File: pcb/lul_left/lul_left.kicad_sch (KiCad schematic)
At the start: 76 parts, among them J1 JST Connector, J2 JST Connector, SW1 SW_Push, SW10 SW_Push, SW11 SW_Push, SW12 SW_Push, SW13 SW_Push, SW14 SW_Push, SW15 SW_Push, SW16 SW_Push, SW17 SW_Push, SW18 SW_Push, SW19 SW_Push, SW2 SW_Push, SW20 SW_Push, SW21 SW_Push, SW22 SW_Push, SW23 SW_Push, SW24 SW_Push, SW25 SW_Push, SW26 SW_Push, SW27 SW_Push, SW28 SW_Push, SW29 SW_Push, SW3 SW_Push, SW30 SW_Push, SW31 SW_Push, SW32 SW_Push, SW33 SW_Push, SW34 SW_Push, SW4 SW_Push, SW5 SW_Push, SW6 SW_Push, SW7 SW_Push, SW8 SW_Push, SW9 SW_Push, U1 nice_nano, U2 nice_nano

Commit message: switches positioned properly
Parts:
- J1, J2: footprint (none) -> Connector_JST:JST_PH_S2B-PH-K_1x02_P2.00mm_Horizontal
- SW1, SW10, SW11, SW12, SW14, SW15, SW16, SW17, SW18, SW19, SW2, SW20, SW21, SW22, SW23, SW24, SW26, SW27, SW28, SW29, SW3, SW30, SW31, SW32, SW33, SW34, SW4, SW5, SW6, SW7, SW8, SW9: footprint zzkeeb:Switch_MX-hotswap -> MX_Only:MXOnly-1U-Hotswap
- SW13, SW25: footprint zzkeeb:Switch_MX-hotswap -> MX_Only:MXOnly-1.75U-Hotswap
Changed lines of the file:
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@@
       (effects (font (size 1.27 1.27)))
     )
-    (property "Footprint" "zzkeeb:Switch_MX-hotswap" (at 41.91 129.54 0)
+    (property "Footprint" "MX_Only:MXOnly-1.75U-Hotswap" (at 41.91 129.54 0)
       (effects (font (size 1.27 1.27)) hide)
     )
@@
       (effects (font (size 1.27 1.27)))
     )
-    (property "Footprint" "zzkeeb:Switch_MX-hotswap" (at 99.06 91.44 0)
+    (property "Footprint" "MX_Only:MXOnly-1U-Hotswap" (at 99.06 91.44 0)
       (effects (font (size 1.27 1.27)) hide)
     )
@@
       (effects (font (size 1.27 1.27)))
     )
-    (property "Footprint" "zzkeeb:Switch_MX-hotswap" (at 41.91 104.14 0)
+    (property "Footprint" "MX_Only:MXOnly-1U-Hotswap" (at 41.91 104.14 0)
       (effects (font (size 1.27 1.27)) hide)
     )
@@
       (effects (font (size 1.27 1.27)))
     )
-    (property "Footprint" "zzkeeb:Switch_MX-hotswap" (at 41.91 25.4 0)
+    (property "Footprint" "MX_Only:MXOnly-1U-Hotswap" (at 41.91 25.4 0)
       (effects (font (size 1.27 1.27)) hide)
     )
@@
       (effects (font (size 1.27 1.27)))
     )
-    (property "Footprint" "zzkeeb:Switch_MX-hotswap" (at 60.96 25.4 0)
+    (property "Footprint" "MX_Only:MXOnly-1U-Hotswap" (at 60.96 25.4 0)
       (effects (font (size 1.27 1.27)) hide)
     )
@@
       (effects (font (size 1.27 1.27)))
     )
-    (property "Footprint" "zzkeeb:Switch_MX-hotswap" (at 80.01 25.4 0)
+    (property "Footprint" "MX_Only:MXOnly-1U-Hotswap" (at 80.01 25.4 0)
       (effects (font (size 1.27 1.27)) hide)
     )
@@
       (effects (font (size 1.27 1.27)))
     )
-    (property "Footprint" "zzkeeb:Switch_MX-hotswap" (at 41.91 116.84 0)
+    (property "Footprint" "MX_Only:MXOnly-1U-Hotswap" (at 41.91 116.84 0)
       (effects (font (size 1.27 1.27)) hide)
     )
@@
       (effects (font (size 1.27 1.27)))
     )
-    (property "Footprint" "zzkeeb:Switch_MX-hotswap" (at 22.86 38.1 0)
+    (property "Footprint" "MX_Only:MXOnly-1U-Hotswap" (at 22.86 38.1 0)
       (effects (font (size 1.27 1.27)) hide)
     )
@@
       (effects (font (size 1.27 1.27)))
     )
-    (property "Footprint" "zzkeeb:Switch_MX-hotswap" (at 80.01 116.84 0)
+    (property "Footprint" "MX_Only:MXOnly-1U-Hotswap" (at 80.01 116.84 0)
       (effects (font (size 1.27 1.27)) hide)
     )
@@
       (effects (font (size 1.27 1.27)))
     )
-    (property "Footprint" "zzkeeb:Switch_MX-hotswap" (at 99.06 50.8 0)
+    (property "Footprint" "MX_Only:MXOnly-1U-Hotswap" (at 99.06 50.8 0)
       (effects (font (size 1.27 1.27)) hide)
     )
@@
       (effects (font (size 1.27 1.27)))
     )
-    (property "Footprint" "zzkeeb:Switch_MX-hotswap" (at 80.01 38.1 0)
+    (property "Footprint" "MX_Only:MXOnly-1U-Hotswap" (at 80.01 38.1 0)
       (effects (font (size 1.27 1.27)) hide)
     )
@@
       (effects (font (size 1.27 1.27)))
     )
-    (property "Footprint" "zzkeeb:Switch_MX-hotswap" (at 60.96 38.1 0)
+    (property "Footprint" "MX_Only:MXOnly-1U-Hotswap" (at 60.96 38.1 0)
       (effects (font (size 1.27 1.27)) hide)
     )
@@
       (effects (font (size 1.27 1.27)))
     )
-    (property "Footprint" "zzkeeb:Switch_MX-hotswap" (at 99.06 25.4 0)
+    (property "Footprint" "MX_Only:MXOnly-1U-Hotswap" (at 99.06 25.4 0)
       (effects (font (size 1.27 1.27)) hide)
     )
@@
       (effects (font (size 1.27 1.27)))
     )
-    (property "Footprint" "zzkeeb:Switch_MX-hotswap" (at 80.01 104.14 0)
+    (property "Footprint" "MX_Only:MXOnly-1U-Hotswap" (at 80.01 104.14 0)
       (effects (font (size 1.27 1.27)) hide)
     )
@@
       (effects (font (size 1.27 1.27)))
     )
-    (property "Footprint" "zzkeeb:Switch_MX-hotswap" (at 80.01 63.5 0)
+    (property "Footprint" "MX_Only:MXOnly-1.75U-Hotswap" (at 80.01 63.5 0)
       (effects (font (size 1.27 1.27)) hide)
     )
@@
       (effects (font (size 1.27 1.27)))
     )
-    (property "Footprint" "zzkeeb:Switch_MX-hotswap" (at 41.91 91.44 0)
+    (property "Footprint" "MX_Only:MXOnly-1U-Hotswap" (at 41.91 91.44 0)
       (effects (font (size 1.27 1.27)) hide)
     )
@@
       (effects (font (size 1.27 1.27)))
     )
-    (property "Footprint" "zzkeeb:Switch_MX-hotswap" (at 60.96 116.84 0)
+    (property "Footprint" "MX_Only:MXOnly-1U-Hotswap" (at 60.96 116.84 0)
       (effects (font (size 1.27 1.27)) hide)
     )
@@
       (effects (font (size 1.27 1.27)))
     )
-    (property "Footprint" "zzkeeb:Switch_MX-hotswap" (at 22.86 116.84 0)
+    (property "Footprint" "MX_Only:MXOnly-1U-Hotswap" (at 22.86 116.84 0)
       (effects (font (size 1.27 1.27)) hide)
     )
@@
       (effects (font (size 1.27 1.27)))
     )
-    (property "Footprint" "zzkeeb:Switch_MX-hotswap" (at 99.06 104.14 0)
+    (property "Footprint" "MX_Only:MXOnly-1U-Hotswap" (at 99.06 104.14 0)
       (effects (font (size 1.27 1.27)) hide)
     )
@@
       (effects (font (size 1.27 1.27)))
     )
-    (property "Footprint" "zzkeeb:Switch_MX-hotswap" (at 99.06 116.84 0)
+    (property "Footprint" "MX_Only:MXOnly-1U-Hotswap" (at 99.06 116.84 0)
       (effects (font (size 1.27 1.27)) hide)
     )
@@
       (effects (font (size 1.27 1.27)))
     )
-    (property "Footprint" "zzkeeb:Switch_MX-hotswap" (at 80.01 91.44 0)
+    (property "Footprint" "MX_Only:MXOnly-1U-Hotswap" (at 80.01 91.44 0)
       (effects (font (size 1.27 1.27)) hide)
     )
@@
       (effects (font (size 1.27 1.27)))
     )
-    (property "Footprint" "zzkeeb:Switch_MX-hotswap" (at 99.06 38.1 0)
+    (property "Footprint" "MX_Only:MXOnly-1U-Hotswap" (at 99.06 38.1 0)
       (effects (font (size 1.27 1.27)) hide)
     )
@@
       (effects (font (size 1.27 1.27)))
     )
-    (property "Footprint" "zzkeeb:Switch_MX-hotswap" (at 80.01 50.8 0)
+    (property "Footprint" "MX_Only:MXOnly-1U-Hotswap" (at 80.01 50.8 0)
       (effects (font (size 1.27 1.27)) hide)
     )
@@
       (effects (font (size 1.27 1.27)))
     )
-    (property "Footprint" "zzkeeb:Switch_MX-hotswap" (at 22.86 129.54 0)
+    (property "Footprint" "MX_Only:MXOnly-1U-Hotswap" (at 22.86 129.54 0)
       (effects (font (size 1.27 1.27)) hide)
     )
@@
       (effects (font (size 1.27 1.27)))
     )
-    (property "Footprint" "zzkeeb:Switch_MX-hotswap" (at 60.96 91.44 0)
+    (property "Footprint" "MX_Only:MXOnly-1U-Hotswap" (at 60.96 91.44 0)
       (effects (font (size 1.27 1.27)) hide)
     )
@@
       (effects (font (size 1.27 1.27)))
     )
-    (property "Footprint" "zzkeeb:Switch_MX-hotswap" (at 60.96 50.8 0)
+    (property "Footprint" "MX_Only:MXOnly-1U-Hotswap" (at 60.96 50.8 0)
       (effects (font (size 1.27 1.27)) hide)
     )
@@
       (effects (font (size 1.27 1.27)))
     )
-    (property "Footprint" "" (at 114.3 161.29 0)
+    (property "Footprint" "Connector_JST:JST_PH_S2B-PH-K_1x02_P2.00mm_Horizontal" (at 114.3 161.29 0)
       (effects (font (size 1.27 1.27)) hide)
     )
@@
       (effects (font (size 1.27 1.27)))
     )
-    (property "Footprint" "zzkeeb:Switch_MX-hotswap" (at 41.91 38.1 0)
+    (property "Footprint" "MX_Only:MXOnly-1U-Hotswap" (at 41.91 38.1 0)
       (effects (font (size 1.27 1.27)) hide)
     )
@@
       (effects (font (size 1.27 1.27)))
     )
-    (property "Footprint" "" (at 74.93 160.02 0)
+    (property "Footprint" "Connector_JST:JST_PH_S2B-PH-K_1x02_P2.00mm_Horizontal" (at 74.93 160.02 0)
       (effects (font (size 1.27 1.27)) hide)
     )
@@
       (effects (font (size 1.27 1.27)))
     )
-    (property "Footprint" "zzkeeb:Switch_MX-hotswap" (at 22.86 25.4 0)
+    (property "Footprint" "MX_Only:MXOnly-1U-Hotswap" (at 22.86 25.4 0)
       (effects (font (size 1.27 1.27)) hide)
     )
@@
       (effects (font (size 1.27 1.27)))
     )
-    (property "Footprint" "zzkeeb:Switch_MX-hotswap" (at 22.86 91.44 0)
+    (property "Footprint" "MX_Only:MXOnly-1U-Hotswap" (at 22.86 91.44 0)
       (effects (font (size 1.27 1.27)) hide)
     )
@@
       (effects (font (size 1.27 1.27)))
     )
-    (property "Footprint" "zzkeeb:Switch_MX-hotswap" (at 60.96 104.14 0)
+    (property "Footprint" "MX_Only:MXOnly-1U-Hotswap" (at 60.96 104.14 0)
       (effects (font (size 1.27 1.27)) hide)
     )
@@
       (effects (font (size 1.27 1.27)))
     )
-    (property "Footprint" "zzkeeb:Switch_MX-hotswap" (at 22.86 104.14 0)
+    (property "Footprint" "MX_Only:MXOnly-1U-Hotswap" (at 22.86 104.14 0)
       (effects (font (size 1.27 1.27)) hide)
     )
@@
       (effects (font (size 1.27 1.27)))
     )
-    (property "Footprint" "zzkeeb:Switch_MX-hotswap" (at 99.06 63.5 0)
+    (property "Footprint" "MX_Only:MXOnly-1U-Hotswap" (at 99.06 63.5 0)
       (effects (font (size 1.27 1.27)) hide)
     )
@@
       (effects (font (size 1.27 1.27)))
     )
-    (property "Footprint" "zzkeeb:Switch_MX-hotswap" (at 22.86 50.8 0)
+    (property "Footprint" "MX_Only:MXOnly-1U-Hotswap" (at 22.86 50.8 0)
       (effects (font (size 1.27 1.27)) hide)
     )
@@
       (effects (font (size 1.27 1.27)))
     )
-    (property "Footprint" "zzkeeb:Switch_MX-hotswap" (at 41.91 50.8 0)
-      (effects (font (size 1.27 1.27)) hide)
-    )
+    (property "Footprint" "MX_Only:MXOnly-1U-Hotswap" (at 41.91 50.8 0)
+      (effects (font (size 1.27 1.27)) hide)
+    )

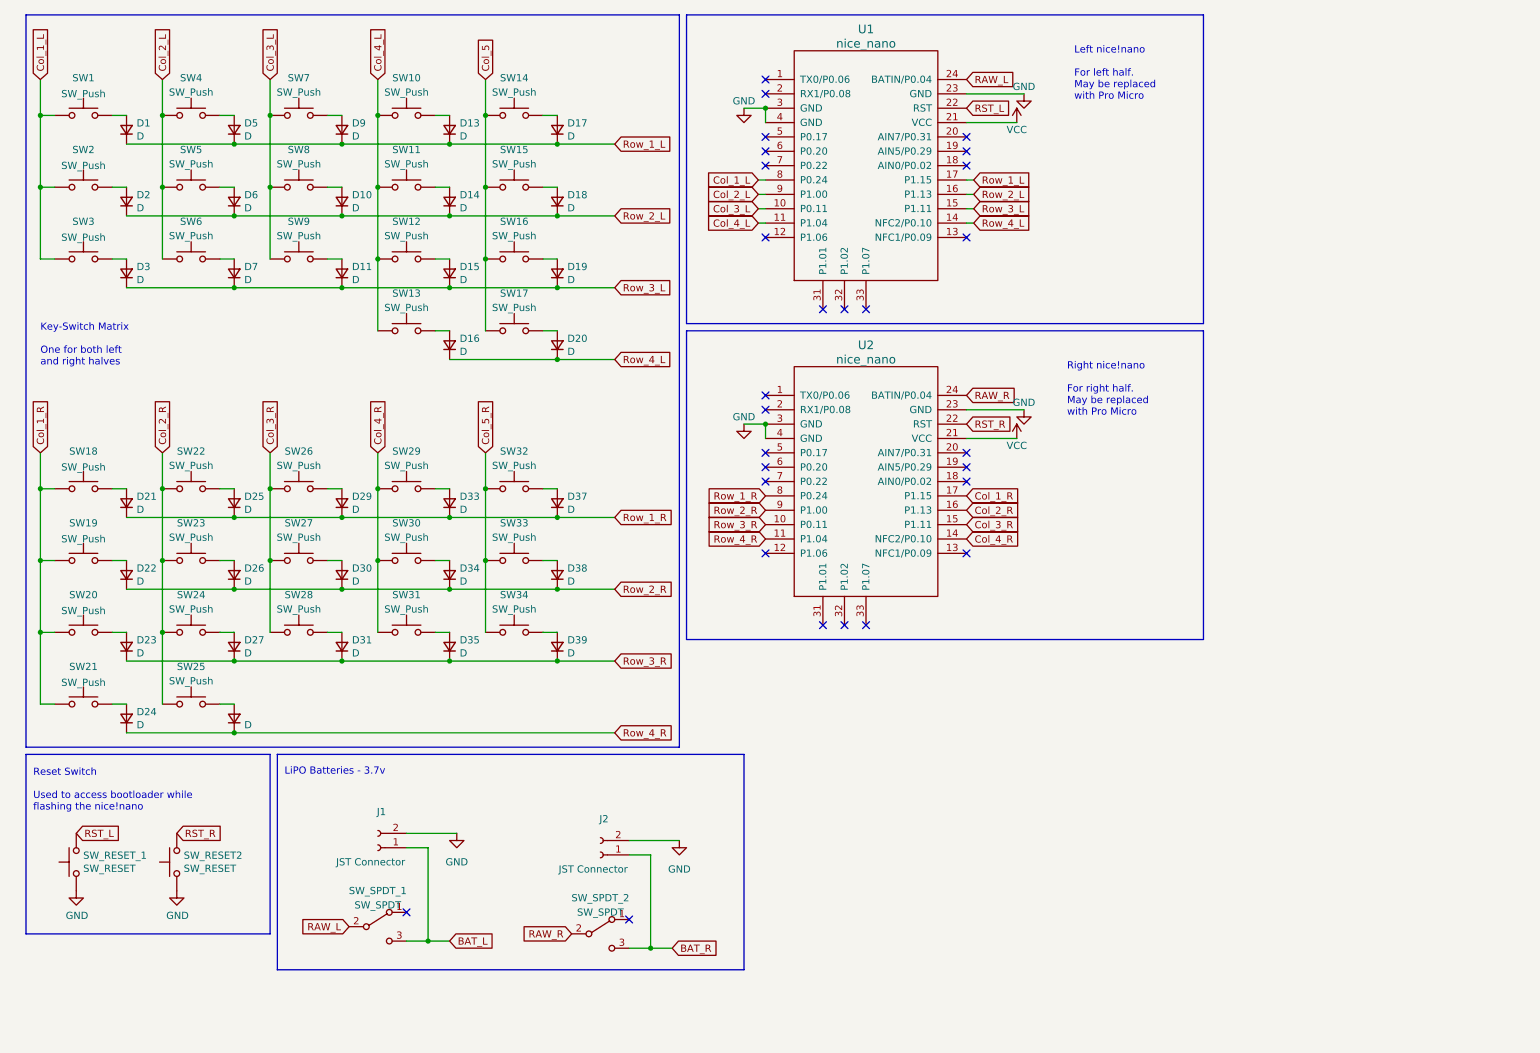
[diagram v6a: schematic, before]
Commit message: change schematic to be diode-less
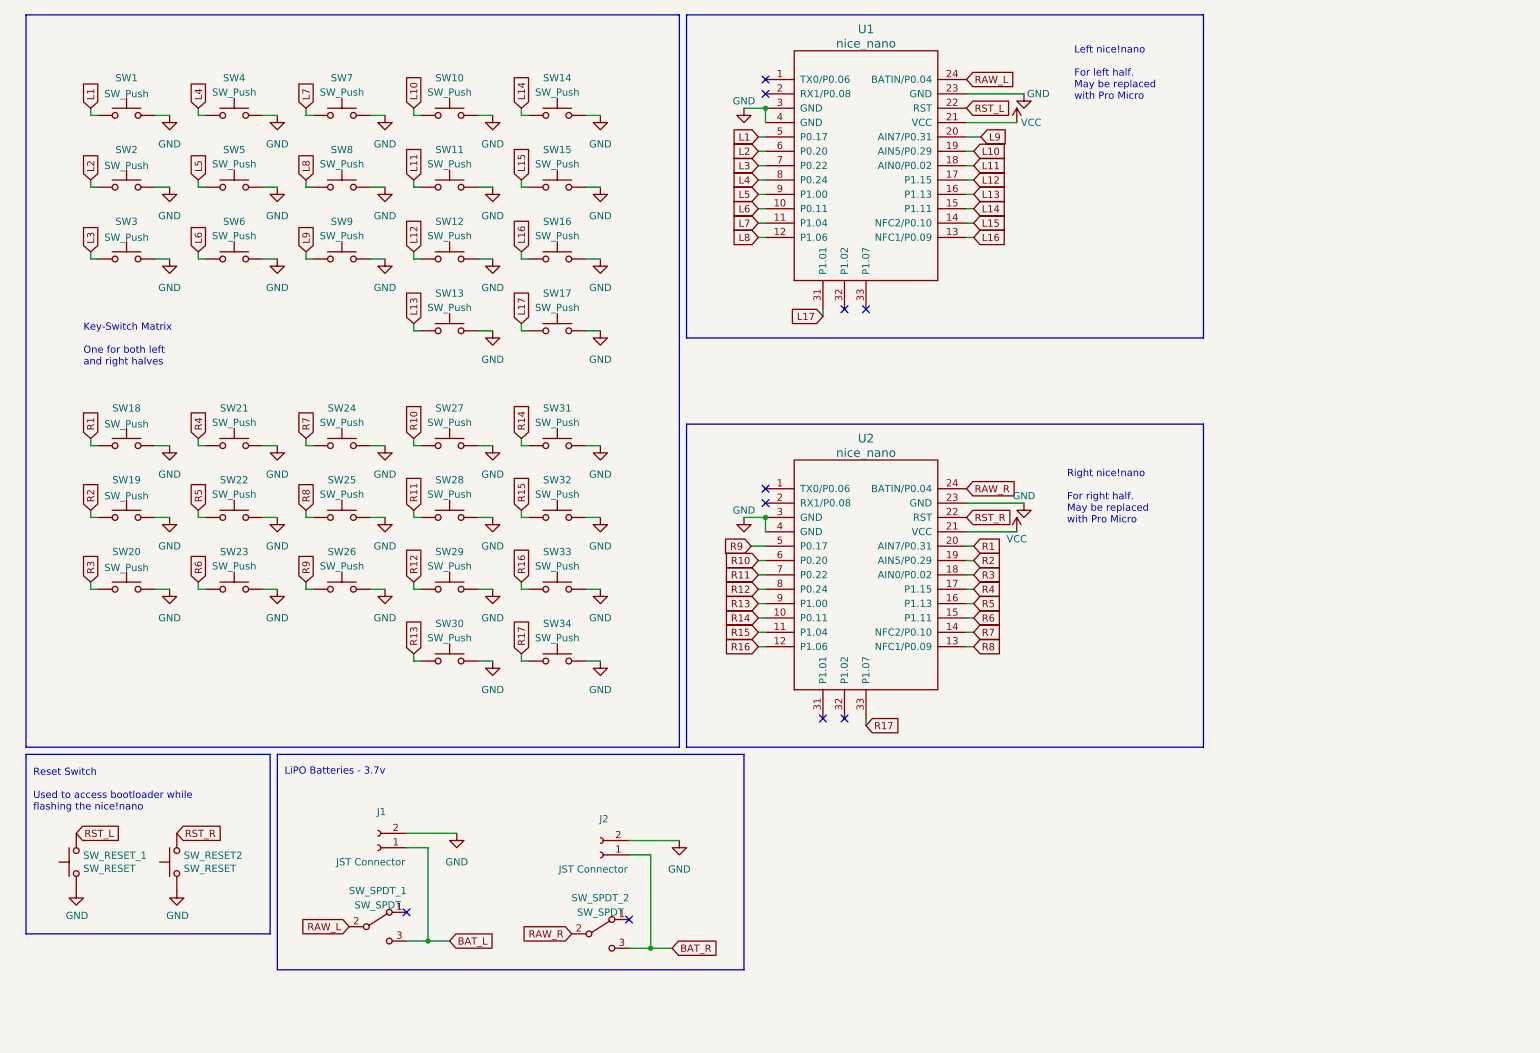
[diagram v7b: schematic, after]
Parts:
- removed D1, D10, D11, D13, D14, D15, D16, D17, D18, D19, D2, D20, D21, D22, D23, D24, D25, D26, D27, D28, D29, D3, D30, D31, D33, D34, D35, D37, D38, D39, D5, D6, D7, D9: D, Diode_SMD:D_SOD-123, symbol Device:D_Small
- SW25: footprint MX_Only:MXOnly-1.75U-Hotswap -> MX_Only:MXOnly-1U-Hotswap
- SW30: footprint MX_Only:MXOnly-1U-Hotswap -> MX_Only:MXOnly-1.75U-Hotswap
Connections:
- net GND: now also SW1.2, SW10.2, SW11.2, SW12.2, SW13.2, SW14.2, SW15.2, SW16.2, SW17.2, SW18.2, SW19.2, SW2.2, SW20.2, SW21.2, SW22.2, SW23.2, SW24.2, SW25.2, SW26.2, SW27.2, SW28.2, SW29.2, SW3.2, SW30.2, SW31.2, SW32.2, SW33.2, SW34.2, SW4.2, SW5.2, SW6.2, SW7.2, SW8.2, SW9.2
- net R16: now reaches U2.12 (P1.06)
- net R16: now also SW33.1
- net R8: now reaches U2.13 (NFC1/P0.09)
- net R8: now also SW25.1
- net R3: now reaches U2.18 (AIN0/P0.02)
- net R3: now also SW20.1
- net R2: now reaches U2.19 (AIN5/P0.29)
- net R2: now also SW19.1
- net R1: now reaches U2.20 (AIN7/P0.31)
- net R1: now also SW18.1
- net R17: now reaches U2.33 (P1.07)
- net R17: now also SW34.1
- net R9: now reaches U2.5 (P0.17)
- net R9: now also SW26.1
- net R10: now reaches U2.6 (P0.20)
- net R10: now also SW27.1
- net R11: now reaches U2.7 (P0.22)
- net R11: now also SW28.1
- net L8: now reaches U1.12 (P1.06)
- net L8: now also SW8.1
- net L16: now reaches U1.13 (NFC1/P0.09)
- net L16: now also SW16.1
- net L11: now reaches U1.18 (AIN0/P0.02)
- net L11: now also SW11.1
- net L10: now reaches U1.19 (AIN5/P0.29)
- net L10: now also SW10.1
- net L9: now reaches U1.20 (AIN7/P0.31)
- net L9: now also SW9.1
- net L17: now reaches U1.31 (P1.01)
- net L17: now also SW17.1
- net L1: now reaches U1.5 (P0.17)
- net L1: now also SW1.1
- net L2: now reaches U1.6 (P0.20)
- net L2: now also SW2.1
- net L3: now reaches U1.7 (P0.22)
- net L3: now also SW3.1
- removed net Col_1_L: SW1.1, SW2.1, SW3.1, U1.8 (P0.24)
- removed net Col_1_R: SW18.1, SW19.1, SW20.1, SW21.1, U2.17 (P1.15)
- net Col_2_L renamed L5
- net L5: no longer SW4.1, SW6.1
- removed net Col_2_R: SW22.1, SW23.1, SW24.1, SW25.1, U2.16 (P1.13)
- removed net Col_3_L: SW7.1, SW8.1, SW9.1, U1.10 (P0.11)
- removed net Col_3_R: SW26.1, SW27.1, SW28.1, U2.15 (P1.11)
- removed net Col_4_L: SW10.1, SW11.1, SW12.1, SW13.1, U1.11 (P1.04)
- removed net Col_4_R: SW29.1, SW30.1, SW31.1, U2.14 (NFC2/P0.10)
- removed net Col_5: SW14.1, SW15.1, SW16.1, SW17.1
- removed net Col_5_R: SW32.1, SW33.1, SW34.1
- net Row_1_L renamed L12
- net L12: now also SW12.1
- net Row_1_R renamed R12
- net R12: now also SW29.1
- net Row_2_L renamed L13
- net L13: now also SW13.1
- net Row_2_R renamed R13
- net R13: now also SW30.1
- net Row_3_L renamed L14
- net L14: now also SW14.1
- net Row_3_R renamed R14
- net R14: now also SW31.1
- net Row_4_L renamed L15
- net L15: now also SW15.1
- net Row_4_R renamed R15
- net R15: now also SW32.1
- new net L4: SW4.1, U1.8 (P0.24)
- new net L6: SW6.1, U1.10 (P0.11)
- new net L7: SW7.1, U1.11 (P1.04)
- new net R4: SW21.1, U2.17 (P1.15)
- new net R5: SW22.1, U2.16 (P1.13)
- new net R6: SW23.1, U2.15 (P1.11)
- new net R7: SW24.1, U2.14 (NFC2/P0.10)
- no-connect marks 28 -> 10
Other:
- moved on the sheet: SW1, SW10, SW11, SW12, SW13, SW14, SW15, SW16, SW17, SW2, SW3, SW4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

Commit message: move components to temporary locations
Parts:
- renumbered SW30 to SW21, SW21 to SW22, SW22 to SW23, SW23 to SW24, SW34 to SW25, SW24 to SW26, SW25 to SW27, SW26 to SW28, SW27 to SW29, SW28 to SW30, SW29 to SW31, SW31 to SW32, SW32 to SW33, SW33 to SW34
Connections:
- net R10: now also SW27.1; no longer SW29.1
- net R11: now also SW28.1; no longer SW30.1
- net R12: now also SW29.1; no longer SW31.1
- net R13: now also SW30.1; no longer SW21.1
- net R14: now also SW31.1; no longer SW32.1
- net R15: now also SW32.1; no longer SW33.1
- net R16: now also SW33.1; no longer SW34.1
- net R17: now also SW34.1; no longer SW25.1
- net R4: now also SW21.1; no longer SW22.1
- net R5: now also SW22.1; no longer SW23.1
- net R6: now also SW23.1; no longer SW24.1
- net R7: now also SW24.1; no longer SW26.1
- net R8: now also SW25.1; no longer SW27.1
- net R9: now also SW26.1; no longer SW28.1
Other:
- moved on the sheet: SW21, SW25
